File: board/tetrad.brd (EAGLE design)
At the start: 100 x 100 mm, 90 parts, among them Q1 FET-PCH-TO252, Q10 FET-NCH-SOT23, Q11 FET-NCH-SOT23, Q12 FET-NCH-SOT23, Q2 FET-NCH-SOT23, Q3 FET-NCH-SOT23, Q4 FET-NCH-SOT23, Q5 FET-NCH-SOT23, Q6 FET-NCH-SOT23, Q7 FET-NCH-SOT23, Q8 FET-NCH-SOT23, Q9 FET-NCH-SOT23, U1 IO-MCP23017SO, U2 RADIO-ESP32_DEVKIT, U3 R-78E5.0-1.0

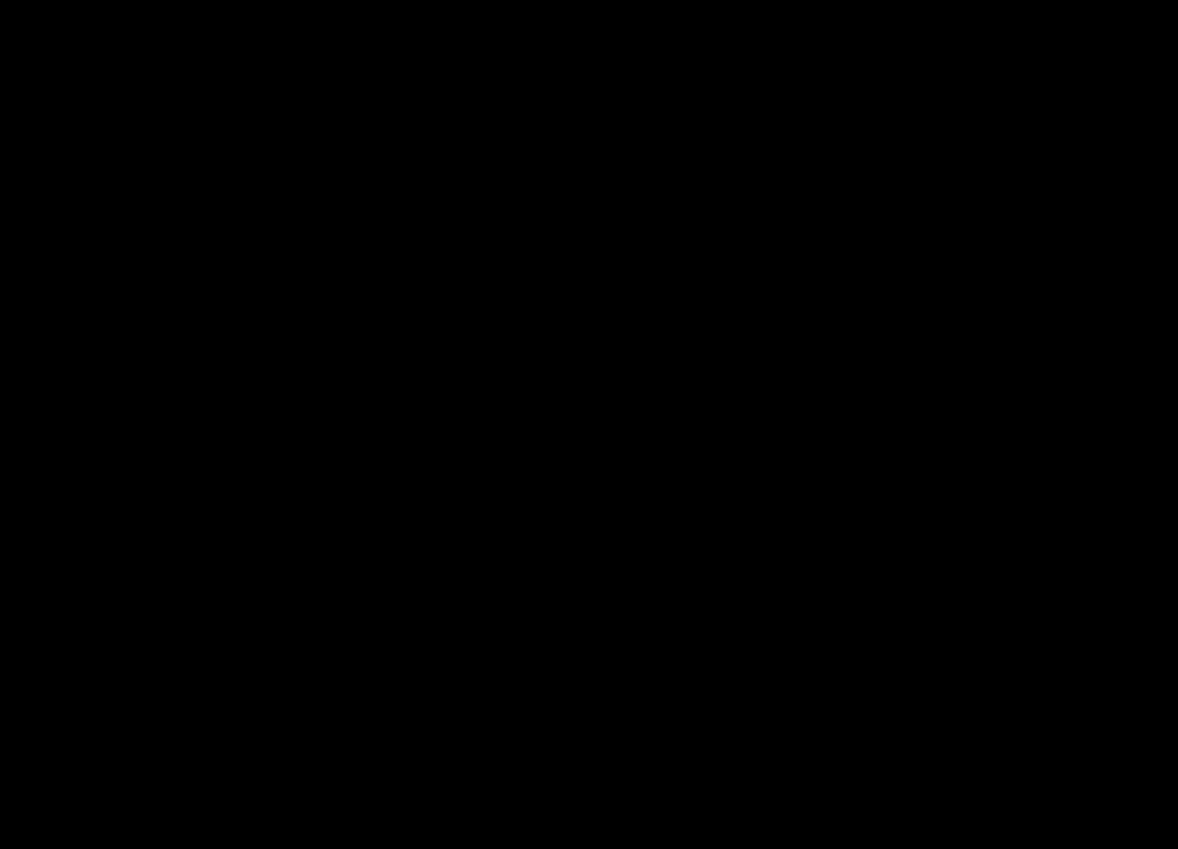
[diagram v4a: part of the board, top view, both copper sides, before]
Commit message: starting add drv8825 slots and micro-fit connectors
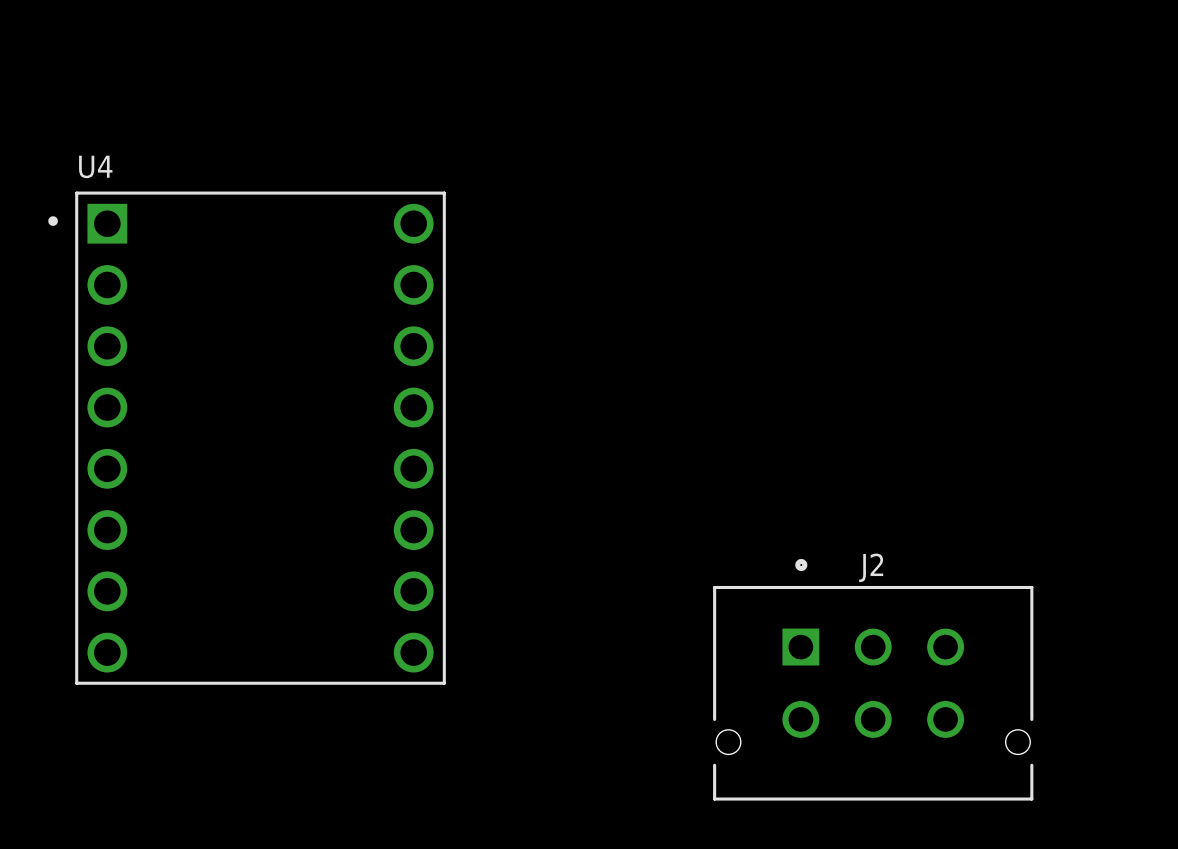
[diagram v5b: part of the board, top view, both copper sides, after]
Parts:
- added J2: CONN-03X2-MICROFIT-430450612, holla:MOLEX_0430450614
- added U4: (no value), holla:IC_DRV8825_STEPPER_MOTOR_DRIVER_CARRIER
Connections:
- new net VMOTOR: U4.16
- net GND: now also U4.15, U4.9
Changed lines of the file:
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@@
 <layer number="14" name="Route14" color="1" fill="6" visible="no" active="no"/>
 <layer number="15" name="Route15" color="4" fill="6" visible="no" active="no"/>
-<layer number="16" name="Bottom" color="1" fill="1" visible="no" active="yes"/>
+<layer number="16" name="Bottom" color="1" fill="1" visible="yes" active="yes"/>
 <layer number="17" name="Pads" color="2" fill="1" visible="yes" active="yes"/>
 <layer number="18" name="Vias" color="2" fill="1" visible="yes" active="yes"/>
@@
 </element>
 <element name="U2" library="holla" package="ESP32_DEVKIT" value="RADIO-ESP32_DEVKIT" x="51.94" y="75.56"/>
+<element name="J2" library="holla" package="MOLEX_0430450614" value="CONN-03X2-MICROFIT-430450612" x="-22.86" y="-7.62">
+<attribute name="PRICE" value="None" x="-22.86" y="-7.62" size="1.778" layer="27" display="off"/>
+<attribute name="MP" value="430450612" x="-22.86" y="-7.62" size="1.778" layer="27" display="off"/>
+<attribute name="MF" value="Molex" x="-22.86" y="-7.62" size="1.778" layer="27" display="off"/>
+<attribute name="PACKAGE" value="None" x="-22.86" y="-7.62" size="1.778" layer="27" display="off"/>
+<attribute name="AVAILABILITY" value="Unavailable" x="-22.86" y="-7.62" size="1.778" layer="27" display="off"/>
+<attribute name="DESCRIPTION" value=" Conn Power HDR 6 POS 3mm Solder ST Thru-Hole 6 Terminal 1 Port Micro-Fit 3.0Ã¢â¢ Tray " x="-22.86" y="-7.62" size="1.778" layer="27" display="off"/>
+</element>
+<element name="U4" library="holla" package="IC_DRV8825_STEPPER_MOTOR_DRIVER_CARRIER" value="" x="-48.26" y="2.54">
+<attribute name="PRICE" value="None" x="-48.26" y="2.54" size="1.778" layer="27" display="off"/>
+<attribute name="MP" value="DRV8825 STEPPER MOTOR DRIVER CARRIER" x="-48.26" y="2.54" size="1.778" layer="27" display="off"/>
+<attribute name="MF" value="Pololu" x="-48.26" y="2.54" size="1.778" layer="27" display="off"/>
+<attribute name="PACKAGE" value="None" x="-48.26" y="2.54" size="1.778" layer="27" display="off"/>
+<attribute name="AVAILABILITY" value="Unavailable" x="-48.26" y="2.54" size="1.778" layer="27" display="off"/>
+<attribute name="DESCRIPTION" value=" Stepper motor controler; IC: DRV8825; 1.5A; Uin mot: 8.2÷45V " x="-48.26" y="2.54" size="1.778" layer="27" display="off"/>
+</element>
 </elements>
 <signals>
@@
 <wire x1="23.5" y1="57.78" x2="33.715" y2="55.94" width="0" layer="19" extent="1-16"/>
 </signal>
-<signal name="GND">
+<signal name="GND" airwireshidden="yes">
 <contactref element="R17" pad="1"/>
 <contactref element="C14" pad="-"/>
@@
 <contactref element="U2" pad="GND@2"/>
 <contactref element="U2" pad="GND@1"/>
+<contactref element="U4" pad="15"/>
+<contactref element="U4" pad="9"/>
+<wire x1="83.5" y1="93.04" x2="86.6" y2="95.54" width="0" layer="19" extent="1-1"/>
+<wire x1="89.53" y1="91.96" x2="86.6" y2="95.54" width="0" layer="19" extent="1-1"/>
+<wire x1="73.4" y1="96.44" x2="83.5" y2="93.04" width="0" layer="19" extent="1-1"/>
+<wire x1="92.91" y1="68.715" x2="89.53" y2="91.96" width="0" layer="19" extent="1-1"/>
+<wire x1="94.975" y1="61.6" x2="92.91" y2="68.715" width="0" layer="19" extent="1-1"/>
+<wire x1="91.4785" y1="51.0921" x2="94.975" y2="61.6" width="0" layer="19" extent="1-1"/>
+<wire x1="90.4785" y1="51.0921" x2="91.4785" y2="51.0921" width="0" layer="19" extent="1-1"/>
+<wire x1="76.2" y1="68.58" x2="92.91" y2="68.715" width="0" layer="19" extent="1-1"/>
+<wire x1="64.64" y1="60.32" x2="76.2" y2="68.58" width="0" layer="19" extent="1-1"/>
+<wire x1="60" y1="55.785" x2="64.64" y2="60.32" width="0" layer="19" extent="1-1"/>
+<wire x1="59.15" y1="68" x2="64.64" y2="60.32" width="0" layer="19" extent="1-1"/>
+<wire x1="59.15" y1="75.365" x2="59.15" y2="68" width="0" layer="19" extent="1-1"/>
+<wire x1="73.478503125" y1="51.0921" x2="64.64" y2="60.32" width="0" layer="19" extent="1-1"/>
+<wire x1="45.85" y1="68" x2="59.15" y2="68" width="0" layer="19" extent="1-1"/>
+<wire x1="45.215" y1="76.635" x2="45.85" y2="68" width="0" layer="19" extent="1-1"/>
+<wire x1="45.85" y1="83" x2="45.215" y2="76.635" width="0" layer="19" extent="1-1"/>
+<wire x1="50.85" y1="88" x2="45.85" y2="83" width="0" layer="19" extent="1-1"/>
+<wire x1="39.24" y1="60.32" x2="45.85" y2="68" width="0" layer="19" extent="1-1"/>
+<wire x1="33.89" y1="84.78" x2="45.85" y2="83" width="0" layer="19" extent="1-1"/>
+<wire x1="32.62" y1="84.78" x2="33.89" y2="84.78" width="0" layer="19" extent="1-1"/>
+<wire x1="31.35" y1="84.78" x2="32.62" y2="84.78" width="0" layer="19" extent="1-1"/>
+<wire x1="28.81" y1="75.22" x2="31.35" y2="84.78" width="0" layer="19" extent="1-1"/>
+<wire x1="26.15" y1="72" x2="28.81" y2="75.22" width="0" layer="19" extent="1-1"/>
+<wire x1="33" y1="95" x2="32.62" y2="84.78" width="0" layer="19" extent="1-1"/>
+<wire x1="27" y1="95" x2="33" y2="95" width="0" layer="19" extent="1-1"/>
+<wire x1="21" y1="95" x2="27" y2="95" width="0" layer="19" extent="1-1"/>
+<wire x1="15" y1="95" x2="21" y2="95" width="0" layer="19" extent="1-1"/>
+<wire x1="11" y1="84.15" x2="15" y2="95" width="0" layer="19" extent="1-1"/>
+<wire x1="11" y1="78.15" x2="11" y2="84.15" width="0" layer="19" extent="1-1"/>
+<wire x1="11" y1="72.15" x2="11" y2="78.15" width="0" layer="19" extent="1-1"/>
+<wire x1="11" y1="66.15" x2="11" y2="72.15" width="0" layer="19" extent="1-1"/>
+<wire x1="5" y1="87" x2="11" y2="84.15" width="0" layer="19" extent="1-1"/>
+<wire x1="5" y1="81" x2="5" y2="87" width="0" layer="19" extent="1-1"/>
+<wire x1="5" y1="75" x2="5" y2="81" width="0" layer="19" extent="1-1"/>
+<wire x1="5" y1="69" x2="5" y2="75" width="0" layer="19" extent="1-1"/>
+<wire x1="5" y1="62" x2="5" y2="69" width="0" layer="19" extent="1-1"/>
+<wire x1="5" y1="55" x2="5" y2="62" width="0" layer="19" extent="1-1"/>
+<wire x1="17.645" y1="62.56" x2="11" y2="66.15" width="0" layer="19" extent="1-1"/>
+<wire x1="42.255" y1="42.905" x2="39.24" y2="60.32" width="0" layer="19" extent="1-1"/>
+<wire x1="36.255" y1="42.905" x2="42.255" y2="42.905" width="0" layer="19" extent="1-1"/>
+<wire x1="29.97" y1="42.895" x2="36.255" y2="42.905" width="0" layer="19" extent="1-1"/>
+<wire x1="44.785" y1="36.715" x2="42.255" y2="42.905" width="0" layer="19" extent="1-1"/>
+<wire x1="43.54" y1="33.365" x2="44.785" y2="36.715" width="0" layer="19" extent="1-1"/>
+<wire x1="22.175" y1="33.365" x2="29.97" y2="42.895" width="0" layer="19" extent="1-1"/>
+<wire x1="32.54" y1="27.715" x2="22.175" y2="33.365" width="0" layer="19" extent="1-1"/>
+<wire x1="34.655" y1="12.38" x2="32.54" y2="27.715" width="0" layer="19" extent="1-1"/>
+<wire x1="30.21" y1="12.38" x2="34.655" y2="12.38" width="0" layer="19" extent="1-1"/>
+<wire x1="27.305" y1="4.445" x2="30.21" y2="12.38" width="0" layer="19" extent="1-1"/>
+<wire x1="18.285" y1="12.045" x2="27.305" y2="4.445" width="0" layer="19" extent="1-1"/>
+<wire x1="13.92" y1="12.045" x2="18.285" y2="12.045" width="0" layer="19" extent="1-1"/>
+<wire x1="10.795" y1="4.445" x2="13.92" y2="12.045" width="0" layer="19" extent="1-1"/>
+<wire x1="46.72" y1="12.38" x2="34.655" y2="12.38" width="0" layer="19" extent="1-1"/>
+<wire x1="51.165" y1="12.38" x2="46.72" y2="12.38" width="0" layer="19" extent="1-1"/>
+<wire x1="43.815" y1="4.445" x2="46.72" y2="12.38" width="0" layer="19" extent="1-1"/>
+<wire x1="63.23" y1="12.38" x2="51.165" y2="12.38" width="0" layer="19" extent="1-1"/>
+<wire x1="67.675" y1="12.38" x2="63.23" y2="12.38" width="0" layer="19" extent="1-1"/>
+<wire x1="60.325" y1="4.445" x2="63.23" y2="12.38" width="0" layer="19" extent="1-1"/>
+<wire x1="79.115" y1="12.375" x2="67.675" y2="12.38" width="0" layer="19" extent="1-1"/>
+<wire x1="83.55" y1="12.38" x2="79.115" y2="12.375" width="0" layer="19" extent="1-1"/>
+<wire x1="87.995" y1="12.38" x2="83.55" y2="12.38" width="0" layer="19" extent="1-1"/>
+<wire x1="76.835" y1="4.445" x2="79.115" y2="12.375" width="0" layer="19" extent="1-1"/>
+<wire x1="8.15" y1="24.715" x2="13.92" y2="12.045" width="0" layer="19" extent="1-1"/>
+<wire x1="6" y1="32.62" x2="8.15" y2="24.715" width="0" layer="19" extent="1-1"/>
+<wire x1="-41.91" y1="8.89" x2="8.15" y2="24.715" width="0" layer="19" extent="1-1"/>
+<wire x1="-41.91" y1="-6.35" x2="-41.91" y2="8.89" width="0" layer="19" extent="1-1"/>
 </signal>
 <signal name="N$24">
@@
 <wire x1="14.23" y1="28.81" x2="14.635" y2="29.215" width="1.016" layer="1"/>
 </signal>
-<signal name="3V3">
+<signal name="3V3" airwireshidden="yes">
 <contactref element="J1" pad="4"/>
 <contactref element="C1" pad="2"/>
@@
 <contactref element="J17" pad="7"/>
 </signal>
+<signal name="VMOTOR">
+<contactref element="U4" pad="16"/>
+</signal>
 </signals>

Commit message: selected hammond enclosure and larger board
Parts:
- added J3, J4, J5, J6, J7: (no value), holla:MOLEX_0430450614
- added U5, U6, U7: (no value), holla:IC_DRV8825_STEPPER_MOTOR_DRIVER_CARRIER
- J2: value CONN-03X2-MICROFIT-430450612 -> (none)
- moved U4 148.6 mm to (97.0, 34.0), turned to 90 degrees
- moved J2 143.0 mm to (114.0, 34.0), turned to 90 degrees
- moved C14 123.9 mm to (-100.8, 46.0)
- moved C15 123.9 mm to (-79.5, 46.0)
- moved D1 123.9 mm to (-79.0, 52.0)
- moved D2 123.9 mm to (-116.4, 34.4)
- moved J24V0 123.9 mm to (-93.0, 58.1)
- moved J3V3 123.9 mm to (-80.7, 58.1)
- moved J5V0 123.9 mm to (-86.7, 58.1)
- moved Q1 123.9 mm to (-108.4, 42.0)
- moved R16 123.9 mm to (-83.0, 52.0)
- moved R17 123.9 mm to (-114.0, 40.0)
- moved U3 123.9 mm to (-90.5, 43.0)
- moved VIN 123.9 mm to (-117.0, 46.0)
- moved 3V3 123.0 mm to (-46.8, 78.7)
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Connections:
- net GND: now also U5.15, U5.9, U6.15, U6.9, U7.15, U7.9
- net VMOTOR: now also U5.16, U6.16, U7.16
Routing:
- net 5V0: track 227.0 -> 0.00 mm, vias 2 -> 0
- net RESET: track 107.4 -> 0.00 mm, vias 1 -> 0
- net Z_DIR: track 86.7 -> 0.00 mm, vias 2 -> 0
- net Z_STEP: track 85.5 -> 0.00 mm, vias 2 -> 0
- net Z_LIMIT: track 83.0 -> 0.00 mm, vias 2 -> 0
- net DISPLAY_DC: track 78.4 -> 0.00 mm, vias 1 -> 0
- net DISPLAY_CS: track 76.8 -> 0.00 mm, vias 1 -> 0
- net Y_DIR: track 76.1 -> 0.00 mm, vias 2 -> 0
- net X_DIR: track 75.1 -> 0.00 mm, vias 2 -> 0
- net SPINDLE_ENABLE: track 74.8 -> 0.00 mm, vias 3 -> 0
- net Y_LIMIT: track 73.1 -> 0.00 mm, vias 2 -> 0
- net SPINDLE_PWM: track 71.4 -> 0.00 mm, vias 1 -> 0
- net Y_STEP: track 68.5 -> 0.00 mm, vias 2 -> 0
- net X_LIMIT: track 68.0 -> 0.00 mm, vias 2 -> 0
- net SPINDLE_DIR: track 66.9 -> 0.00 mm, vias 1 -> 0
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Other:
- board size 100 x 100 mm -> 122 x 122 mm

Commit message: started initial positioning
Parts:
- J2, J3, J4, J5, J6, J7: device holla:MOLEX_0430450614 -> holla:MOLEX_430450614_430450615
- U1: value IO-MCP23017SO -> IO-MCP23017ML; device holla:SO28W -> holla:QFN28-ML_6X6MM
- U4, U5, U6, U7: device holla:IC_DRV8825_STEPPER_MOTOR_DRIVER_CARRIER -> holla:IC_DRV8825_CARRIER_TH_SMD
- moved J6 288.5 mm to (96.0, 111.0), turned to 90 degrees
- moved J2 24.5 mm to (115.0, 9.50)
- moved U4 24.5 mm to (98.0, 9.50)
- moved J3 16.0 mm to (115.0, 36.0)
- moved U5 16.0 mm to (98.0, 36.0)
- moved J4 10.0 mm to (115.0, 60.0)
- moved U6 10.0 mm to (98.0, 60.0)
- moved J5 3.16 mm to (115.0, 85.0)
- moved U7 3.16 mm to (98.0, 85.0)
- moved U1 2.24 mm to (-100.0, 81.0), turned to 90 degrees
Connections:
- net 3V3: now also U1.5; no longer U1.9
- net DISPLAY_CS: now also U1.21; no longer U1.25
- net DISPLAY_DC: now also U1.22; no longer U1.26
- net GND: now also U1.11, U1.12, U1.13, U1.6, U4.15_, U4.9_, U5.15_, U5.9_, U6.15_, U6.9_, U7.15_, U7.9_; no longer U1.10, U1.15, U1.16, U1.17
- net N$12: now also U1.17; no longer U1.21
- net N$15: now also U1.18; no longer U1.22
- net N$22: now also U1.19; no longer U1.23
- net N$23: now also U1.20; no longer U1.24
- net RESET: now also U1.14; no longer U1.18
- net SCL: now also U1.8; no longer U1.12
- net SDA: now also U1.9; no longer U1.13
- net USER0: now also U1.25; no longer U1.1
- net USER1: now also U1.26; no longer U1.2
- net USER2: now also U1.27; no longer U1.3
- net USER3: now also U1.28; no longer U1.4
- net VMOTOR: now also U4.16_, U5.16_, U6.16_, U7.16_

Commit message: started placement of X
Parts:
- removed J3, J4, J5, J6: (no value), holla:MOLEX_430450614_430450615
- removed U4, U5, U6, U7: (no value), holla:IC_DRV8825_CARRIER_TH_SMD
- added C16: 47u, holla:C-1206
- added R28, R30, R32, R34, R36, R38, R40, R42, R44, R46, R48, R50, R52, R54, R56, R58: 0, holla:R-0603
- added R37, R39, R41, R43, R45, R47, R49, R51, R53, R55, R57, R59, RXM0, RXM1, RXM2: DNP, holla:R-0603
- added UA, UX, UY, UZ: (no value), holla:IC_DRV8825_CARRIER_TH_SMD
- A, X, Y, Z: device holla:CONN-.100-6 -> holla:MOLEX_430450614_430450615
- moved X 227.2 mm to (114.9, 9.53), turned to 90 degrees
- moved Y 213.0 mm to (115.0, 36.0), turned to 90 degrees
- moved Z 210.2 mm to (115.0, 85.0), turned to 90 degrees
- moved A 191.1 mm to (96.0, 111.0), turned to 90 degrees
- moved Q11 183.4 mm to (73.3, 9.40), turned to 270 degrees
- moved Q12 182.0 mm to (76.2, 6.99), turned to 270 degrees
- moved J2 45.8 mm to (154.0, 33.5)
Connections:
- removed net VMOTOR: U4.16, U4.16_, U5.16, U5.16_, U6.16, U6.16_, U7.16, U7.16_
- removed net X_STEP_5V0: Q12.3, X.3
- new net AA1: UA.12, UA.12_
- new net AA2: UA.11, UA.11_
- new net AB1: UA.13, UA.13_
- new net AB2: UA.14, UA.14_
- new net N$21: Q12.3, R32.2, UX.7, UX.7_
- new net N$25: R34.2, UX.11, UX.11_, X.6, X.6_
- new net N$30: R28.1, UX.12, UX.12_, X.3, X.3_
- new net N$31: R32.1, UX.13, UX.13_, X.2, X.2_
- new net N$32: R30.1, UX.14, UX.14_, X.1, X.1_
- new net N$33: RXM0.1, UX.2, UX.2_
- new net N$34: RXM1.1, UX.3, UX.3_
- new net N$35: RXM2.1, UX.4, UX.4_
- new net VMGND: UA.15, UA.15_, UY.15, UY.15_, UZ.15, UZ.15_
- new net YA1: UY.12, UY.12_
- new net YA2: UY.11, UY.11_
- new net YB1: UY.13, UY.13_
- new net YB2: UY.14, UY.14_
- new net ZA1: UZ.12, UZ.12_
- new net ZA2: UZ.11, UZ.11_
- new net ZB1: UZ.13, UZ.13_
- new net ZB2: UZ.14, UZ.14_
- net 24V0: now also C16.1, R28.2, UA.16, UA.16_, UX.16, UX.16_, UY.16, UY.16_, UZ.16, UZ.16_; no longer A.6, X.6, Y.6, Z.6
- net 3V3: now also RXM0.2, RXM1.2, RXM2.2, UX.5, UX.5_, UX.6, UX.6_
- net 5V0: now also A.1, A.1_, R30.2, UX.10, UX.10_, Y.1, Y.1_, Z.1, Z.1_; no longer A.5, X.5, Y.5, Z.5
- net GND: now also A.4, A.4_, C16.2, UA.9, UA.9_, UX.15, UX.15_, UX.9, UX.9_, UY.9, UY.9_, UZ.9, UZ.9_, X.4, X.4_, Y.4, Y.4_, Z.4, Z.4_; no longer A.1, U4.15, U4.15_, U4.9, U4.9_, U5.15, U5.15_, U5.9, U5.9_, U6.15, U6.15_, U6.9, U6.9_, U7.15, U7.15_, U7.9, U7.9_, X.1, Y.1, Z.1
- net N$10: no longer A.4
- net N$11: no longer A.2
- net N$2: now also X.5, X.5_; no longer X.4
- net N$5: now also R34.1, UX.8, UX.8_; no longer X.2
- net N$6: no longer Y.4
- net N$7: no longer Y.2
- net N$8: no longer Z.4
- net N$9: no longer Z.2
- net X_STEP_5V1: no longer Y.3
- net X_STEP_5V2: no longer Z.3
- net X_STEP_5V3: no longer A.3
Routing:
- net N$25: track 0.00 -> 54.3 mm, vias 0 -> 1
- net N$2: track 0.00 -> 51.2 mm
- net N$32: track 0.00 -> 46.2 mm, vias 0 -> 1
- net N$5: track 0.00 -> 38.3 mm, vias 0 -> 2
- net N$31: track 0.00 -> 36.6 mm
- net N$21: track 0.00 -> 33.8 mm
- net N$30: track 0.00 -> 32.1 mm
- net 24V0: track 0.00 -> 27.1 mm
- net N$35: track 0.00 -> 15.8 mm
- net N$34: track 0.00 -> 11.9 mm
- net N$33: track 0.00 -> 8.70 mm
